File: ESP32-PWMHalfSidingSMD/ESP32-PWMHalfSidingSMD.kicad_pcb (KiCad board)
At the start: 2 copper layers, 82.5 x 113 mm, 73 parts, among them IC1 MCT6H, IC2 MCT6H, J1 RJ45, J2 RJ45, P601 C A0 A1 A2 A3 A4 A5 A6 A7, P602 C B0 B1 B2 B3 B4 B5 B6 B7, Q1 MMBT3904, Q2 MMBT3904, T1 + 15 in -, T2 + 15 out -, T3 In Track1 Out, T4 Motor 1, T5 Motor 2, T6 In Track1 Out, T601 + 12V -, U0 ESP32_DEVKIT_C or TTGO-T1, U1 TCAN332DR, U3 LM2574N-5.0, U601 PCA9685, U602 TBD62X83A, U603 TBD62X83A, U7 TC4428, U8 TC4428, U9 74HCT00

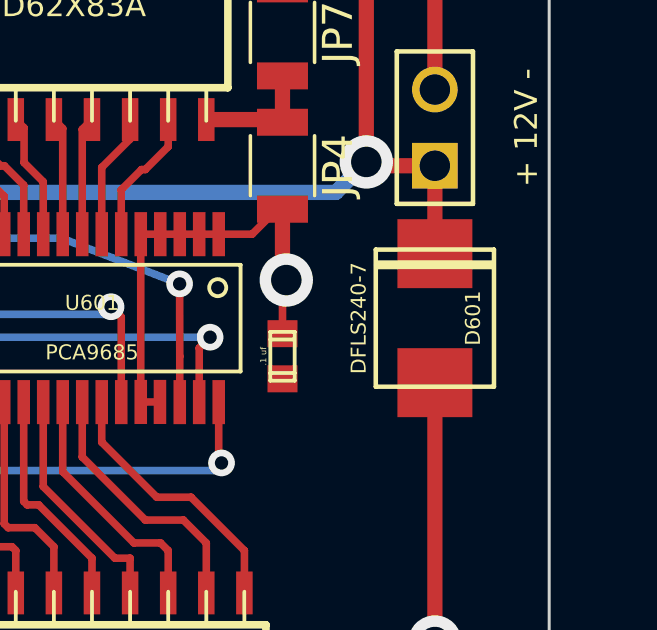
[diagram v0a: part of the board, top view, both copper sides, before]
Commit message: Updates for fabrication of ESP32-PWMHalfSidingSMD.
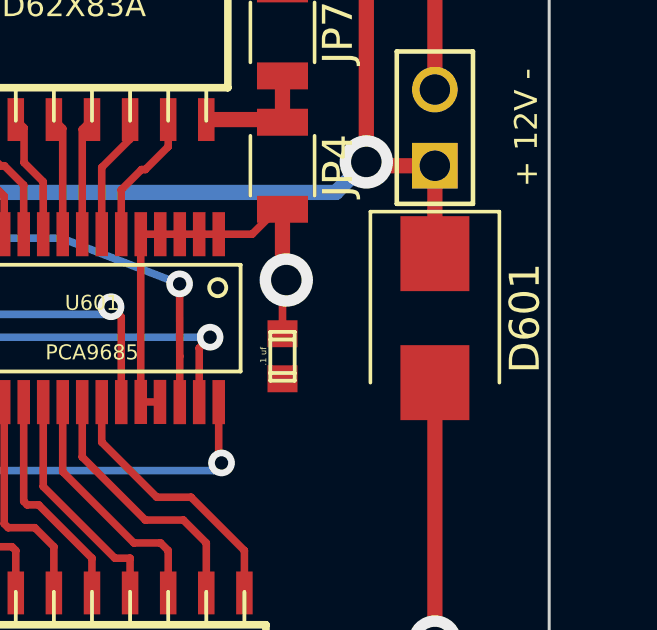
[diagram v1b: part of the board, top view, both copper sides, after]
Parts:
- D601: footprint SMB -> Diodes_SMD:D_SMB
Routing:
- net +12V: track 64.6 -> 114.7 mm, vias 2 -> 4
- net CAN +12V: track 229.3 -> 179.2 mm, vias 7 -> 5
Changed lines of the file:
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@@
   (general
     (links 219)
-    (no_connects 0)
-    (area 96.469999 30.429999 179.120001 143.560001)
+    (no_connects 2)
+    (area 74.90163 20.160001 206.684286 157.64)
     (thickness 1.6)
     (drawings 25)
@@
     (0 F.Cu signal)
     (31 B.Cu signal)
-    (32 B.Adhes user)
     (33 F.Adhes user)
-    (34 B.Paste user)
     (35 F.Paste user)
-    (36 B.SilkS user)
     (37 F.SilkS user)
-    (38 B.Mask user)
     (39 F.Mask user)
     (40 Dwgs.User user)
@@
     (43 Eco2.User user)
     (44 Edge.Cuts user)
+    (45 Margin user)
+    (47 F.CrtYd user)
+    (49 F.Fab user)
   )
   (setup
@@
     (visible_elements 7FFFFFFF)
     (pcbplotparams
-      (layerselection 0x00030_80000001)
+      (layerselection 0x2bfaa_80000001)
       (usegerberextensions true)
       (excludeedgelayer true)
@@
       (drillshape 0)
       (scaleselection 1)
-      (outputdirectory Geber/))
+      (outputdirectory Gerber/))
   )
   (net 0 "")
@@
   (module DWSLogoBCU (layer F.Cu)
     (at 105.664 32.766 180)
+    (attr smd)
     (fp_text reference "" (at 0 0 180) (layer F.SilkS)
       (effects (font (thickness 0.15)))
@@
       (net 46 "Net-(P601-Pad1)"))
   )
-  (module SMB (layer F.Cu)
-    (at 175.26 96.52 270)
-    (attr smd)
-    (fp_text reference D601 (at 0 -1.27 270) (layer F.SilkS)
-      (effects (font (size 0.5 0.5) (thickness 0.075)))
-    )
-    (fp_text value DFLS240-7 (at 0 2.54 270) (layer F.SilkS)
-      (effects (font (size 0.5 0.5) (thickness 0.075)))
-    )
-    (fp_line (start -1.778 -1.89) (end -1.778 1.89) (layer F.SilkS) (width 0.3))
-    (fp_line (start -2.285 -1.97) (end 2.285 -1.97) (layer F.SilkS) (width 0.15))
-    (fp_line (start 2.285 -1.97) (end 2.285 1.97) (layer F.SilkS) (width 0.15))
-    (fp_line (start 2.285 1.97) (end -2.285 1.97) (layer F.SilkS) (width 0.15))
-    (fp_line (start -2.285 1.97) (end -2.285 -1.97) (layer F.SilkS) (width 0.15))
-    (pad 1 smd rect (at 2.15 0 270) (size 2.3 2.5) (layers F.Cu F.Paste F.Mask)
-      (net 18 "CAN +12V"))
-    (pad 2 smd rect (at -2.15 0 270) (size 2.3 2.5) (layers F.Cu F.Paste F.Mask)
-      (net 1 +12V))
-  )
   (module SM0603 (layer F.Cu)
     (at 121.285 119.634)
@@
       (effects (font (size 1 1) (thickness 0.15)))
     )
-    (fp_text value MMBT3904 (at 0 2.5) (layer F.Fab)
+    (fp_text value MMBT3904 (at 0 -2.22) (layer F.Fab)
       (effects (font (size 1 1) (thickness 0.15)))
     )
@@
       (effects (font (size 1 1) (thickness 0.15)))
     )
-    (fp_text value MMBT3904 (at 0 2.5) (layer F.Fab)
+    (fp_text value MMBT3904 (at 0 -2.286) (layer F.Fab)
       (effects (font (size 1 1) (thickness 0.15)))
     )
@@
     (descr "Fiducial, Classical, Small, Copper Top, Typ 1, Passermarke,")
     (tags "Fiducial, Classical, Small, Copper Top, Typ 1, Passermarke,")
+    (attr smd)
     (fp_text reference REF** (at 0 -3.556) (layer F.SilkS)
       (effects (font (size 1 1) (thickness 0.15)))
@@
     (descr "Fiducial, Classical, Small, Copper Top, Typ 1, Passermarke,")
     (tags "Fiducial, Classical, Small, Copper Top, Typ 1, Passermarke,")
+    (attr smd)
     (fp_text reference REF** (at 0 -3.556) (layer F.SilkS)
       (effects (font (size 1 1) (thickness 0.15)))
@@
     (descr "Fiducial, Classical, Small, Copper Top, Typ 1, Passermarke,")
     (tags "Fiducial, Classical, Small, Copper Top, Typ 1, Passermarke,")
+    (attr smd)
     (fp_text reference REF** (at 0 -3.556) (layer F.SilkS)
       (effects (font (size 1 1) (thickness 0.15)))
@@
   (module LCC_LOGO:LCC_LOGO_4.5x4.5 (layer F.Cu)
     (at 153.924 131.064)
+    (attr smd)
     (fp_text reference G*** (at 0 0) (layer F.SilkS) hide
       (effects (font (thickness 0.3)))
@@
       (effects (font (size 1 1) (thickness 0.15)))
     )
-    (fp_text value "22 uf 100V" (at 0 -5.45 90) (layer F.Fab)
+    (fp_text value "22 uf 100V" (at 0 6.35 90) (layer F.Fab)
       (effects (font (size 1 1) (thickness 0.15)))
     )
@@
       (net 27 "Net-(D5-Pad1)"))
   )
+  (module Diodes_SMD:D_SMB (layer F.Cu)
+    (at 175.26 96.52 270)
+    (descr "Diode SMB (DO-214AA)")
+    (tags "Diode SMB (DO-214AA)")
+    (attr smd)
+    (fp_text reference D601 (at 0 -3 270) (layer F.SilkS)
+      (effects (font (size 1 1) (thickness 0.15)))
+    )
+    (fp_text value DFLS240-7 (at 0 3.1 270) (layer F.Fab)
+      (effects (font (size 1 1) (thickness 0.15)))
+    )
+    (fp_text user %R (at 0 -3 270) (layer F.Fab)
+      (effects (font (size 1 1) (thickness 0.15)))
+    )
+    (fp_line (start -3.55 -2.15) (end -3.55 2.15) (layer F.SilkS) (width 0.12))
+    (fp_line (start 2.3 2) (end -2.3 2) (layer F.Fab) (width 0.1))
+    (fp_line (start -2.3 2) (end -2.3 -2) (layer F.Fab) (width 0.1))
+    (fp_line (start 2.3 -2) (end 2.3 2) (layer F.Fab) (width 0.1))
+    (fp_line (start 2.3 -2) (end -2.3 -2) (layer F.Fab) (width 0.1))
+    (fp_line (start -3.65 -2.25) (end 3.65 -2.25) (layer F.CrtYd) (width 0.05))
+    (fp_line (start 3.65 -2.25) (end 3.65 2.25) (layer F.CrtYd) (width 0.05))
+    (fp_line (start 3.65 2.25) (end -3.65 2.25) (layer F.CrtYd) (width 0.05))
+    (fp_line (start -3.65 2.25) (end -3.65 -2.25) (layer F.CrtYd) (width 0.05))
+    (fp_line (start -0.64944 0.00102) (end -1.55114 0.00102) (layer F.Fab) (width 0.1))
+    (fp_line (start 0.50118 0.00102) (end 1.4994 0.00102) (layer F.Fab) (width 0.1))
+    (fp_line (start -0.64944 -0.79908) (end -0.64944 0.80112) (layer F.Fab) (width 0.1))
+    (fp_line (start 0.50118 0.75032) (end 0.50118 -0.79908) (layer F.Fab) (width 0.1))
+    (fp_line (start -0.64944 0.00102) (end 0.50118 0.75032) (layer F.Fab) (width 0.1))
+    (fp_line (start -0.64944 0.00102) (end 0.50118 -0.79908) (layer F.Fab) (width 0.1))
+    (fp_line (start -3.55 2.15) (end 2.15 2.15) (layer F.SilkS) (width 0.12))
+    (fp_line (start -3.55 -2.15) (end 2.15 -2.15) (layer F.SilkS) (width 0.12))
+    (pad 1 smd rect (at -2.15 0 270) (size 2.5 2.3) (layers F.Cu F.Paste F.Mask)
+      (net 18 "CAN +12V"))
+    (pad 2 smd rect (at 2.15 0 270) (size 2.5 2.3) (layers F.Cu F.Paste F.Mask)
+      (net 1 +12V))
+    (model ${KISYS3DMOD}/Diodes_SMD.3dshapes/D_SMB.wrl
+      (at (xyz 0 0 0))
+      (scale (xyz 1 1 1))
+      (rotate (xyz 0 0 0))
+    )
+  )
   (dimension 105.41 (width 0.3) (layer Cmts.User)
     (gr_text "105.410 mm" (at 194.389999 86.995001 270) (layer Cmts.User)
@@
   (segment (start 171.958 92.329) (end 155.194 92.329) (width 0.508) (layer B.Cu) (net 1))
   (via (at 155.194 92.329) (size 1.778) (drill 1.016) (layers F.Cu B.Cu) (net 1))
+  (segment (start 175.26 107.315) (end 175.26 98.67) (width 0.508) (layer F.Cu) (net 1))
+  (via (at 175.26 107.315) (size 1.778) (drill 1.016) (layers F.Cu B.Cu) (net 1))
+  (segment (start 162.56 107.315) (end 175.26 107.315) (width 0.508) (layer B.Cu) (net 1))
+  (segment (start 150.495 119.38) (end 162.56 107.315) (width 0.508) (layer B.Cu) (net 1))
+  (segment (start 139.7 119.38) (end 150.495 119.38) (width 0.508) (layer B.Cu) (net 1))
+  (segment (start 139.065 120.015) (end 139.7 119.38) (width 0.508) (layer B.Cu) (net 1))
+  (via (at 139.065 120.015) (size 1.778) (drill 1.016) (layers F.Cu B.Cu) (net 1))
   (segment (start 126.619 110.871) (end 124.46 113.03) (width 0.508) (layer B.Cu) (net 2))
   (segment (start 128.524 110.871) (end 126.619 110.871) (width 0.508) (layer B.Cu) (net 2))
@@
   (segment (start 148.971 45.212) (end 148.844 45.085) (width 0.508) (layer B.Cu) (net 18))
   (segment (start 137.16 122.6312) (end 137.16 121.92) (width 0.508) (layer F.Cu) (net 18))
-  (segment (start 175.26 107.315) (end 175.26 98.67) (width 0.508) (layer F.Cu) (net 18))
-  (via (at 175.26 107.315) (size 1.778) (drill 1.016) (layers F.Cu B.Cu) (net 18))
-  (segment (start 162.56 107.315) (end 175.26 107.315) (width 0.508) (layer B.Cu) (net 18))
-  (segment (start 150.495 119.38) (end 162.56 107.315) (width 0.508) (layer B.Cu) (net 18))
-  (segment (start 139.7 119.38) (end 150.495 119.38) (width 0.508) (layer B.Cu) (net 18))
-  (segment (start 139.065 120.015) (end 139.7 119.38) (width 0.508) (layer B.Cu) (net 18))
-  (via (at 139.065 120.015) (size 1.778) (drill 1.016) (layers F.Cu B.Cu) (net 18))
   (segment (start 137.16 121.92) (end 139.065 120.015) (width 0.508) (layer F.Cu) (net 18))
   (segment (start 129.54 53.975) (end 148.336 53.975) (width 0.508) (layer B.Cu) (net 18))

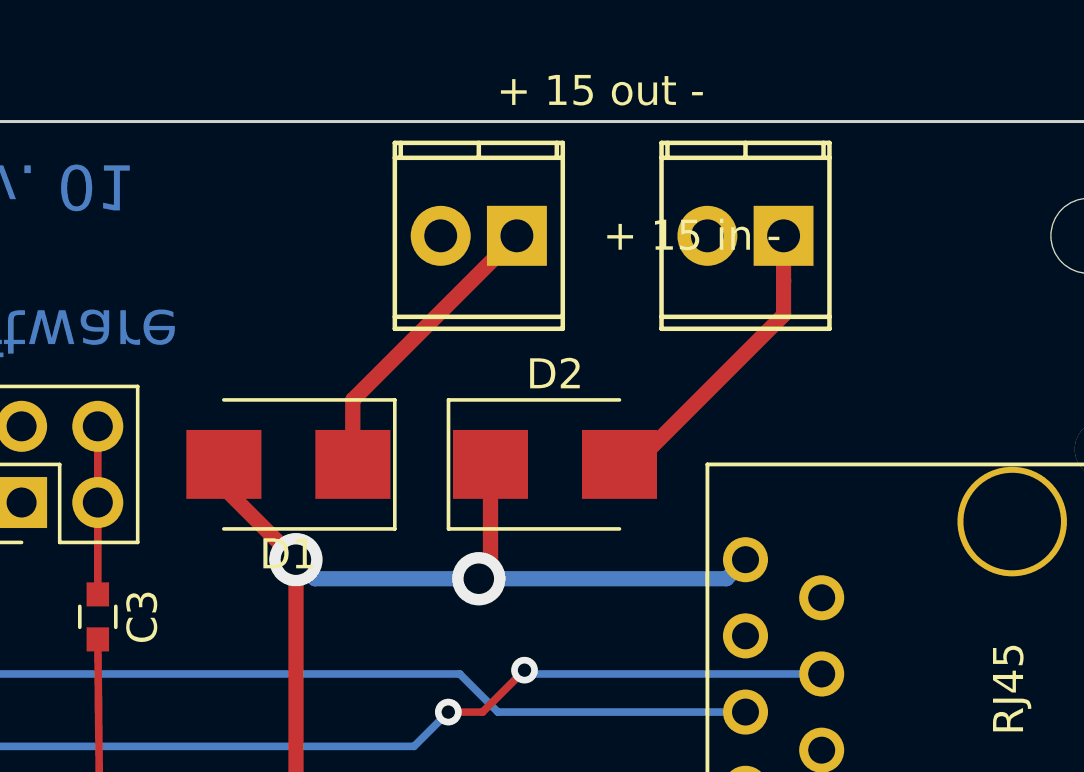
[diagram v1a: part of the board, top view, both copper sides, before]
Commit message: Add 3D files for the through hole parts and update documenation for ESP32-PWMHalfSidingSMD.
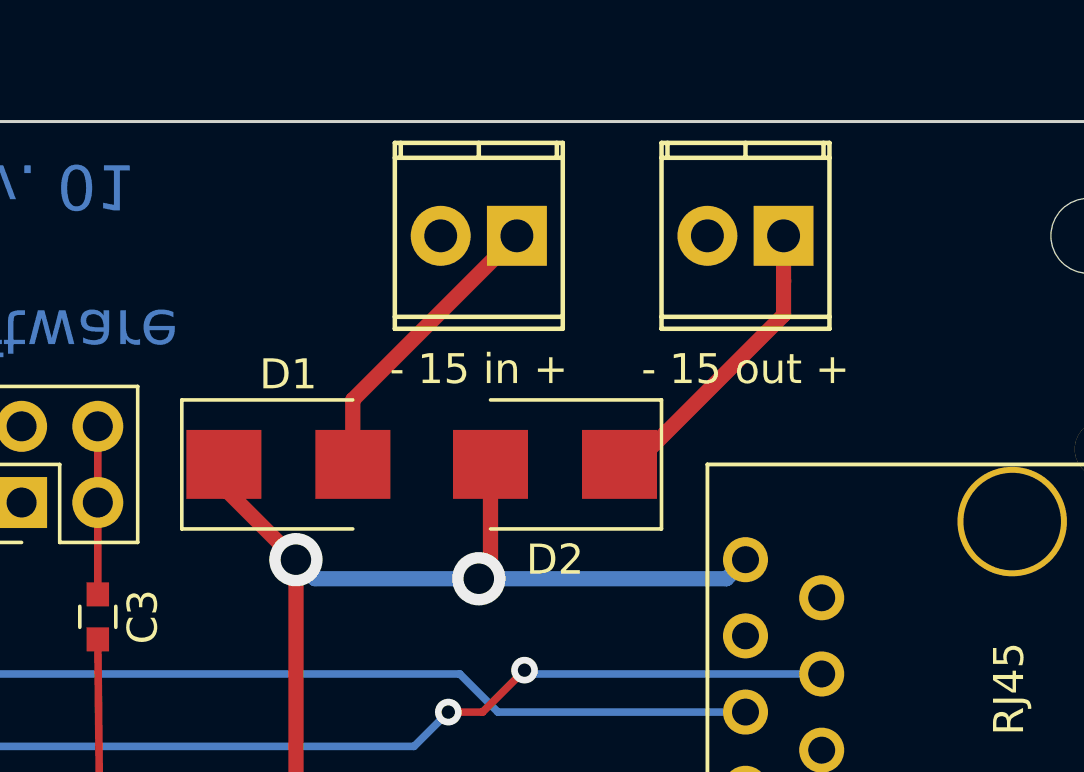
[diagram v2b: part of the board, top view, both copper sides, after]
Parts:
- T1: value + 15 in - -> - 15 in +
- T2: value + 15 out - -> - 15 out +
- turned D1 to 0 degrees
- turned D2 to 180 degrees
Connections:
- U7 pad 6: CAN +12V -> Vdd
- U8 pad 6: CAN +12V -> Vdd
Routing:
- net CAN +12V: track 179.2 -> 169.2 mm
- net Vdd: track 0.00 -> 10.1 mm

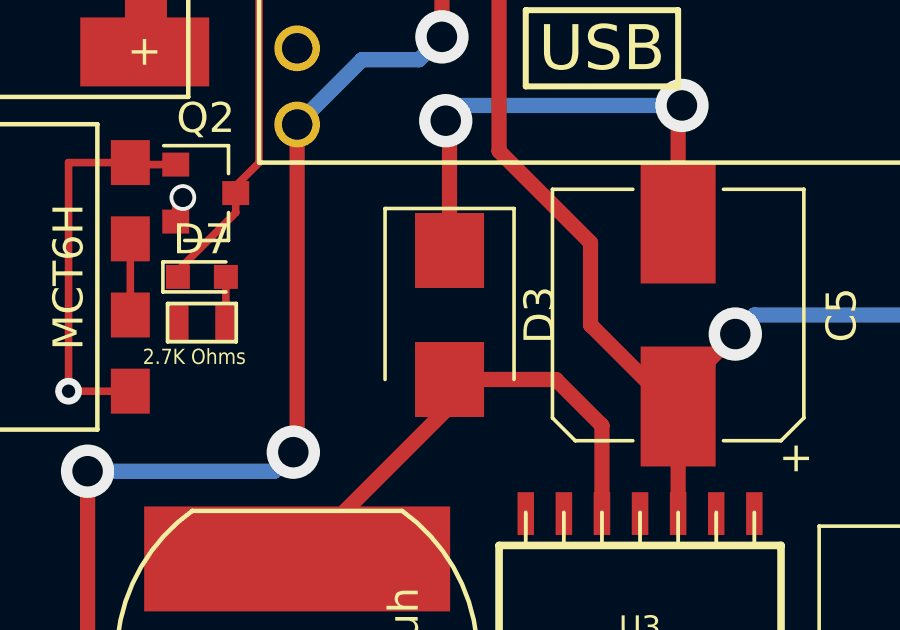
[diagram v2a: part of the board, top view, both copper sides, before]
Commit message: Final adjustments (update backwards diode footprints).
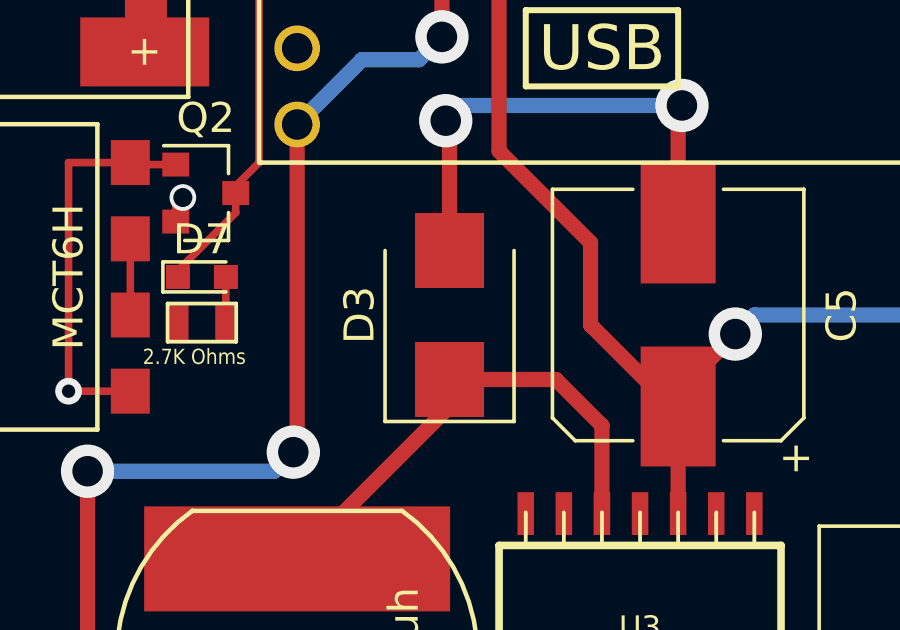
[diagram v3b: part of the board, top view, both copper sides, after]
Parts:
- turned D3 to 90 degrees
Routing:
- net CAN +12V: track 169.2 -> 173.9 mm
- net Net-(D2-Pad2): track 9.68 -> 4.93 mm
